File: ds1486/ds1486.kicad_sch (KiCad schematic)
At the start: 13 parts, among them J2 DBG1-16, J3 DBG17-32, J4 DS1-16, J5 DS17-32, U1 RP2040, U2 FXMA108, U3 AMS1117-3.3, Y2 E3SB12E00004EE

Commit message: PCB without RTC and battery.
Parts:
- removed U2: FXMA108, Package_DFN_QFN:WQFN-20-1EP_2.5x4.5mm_P0.5mm_EP1x2.9mm, symbol Logic_LevelTranslator:FXMA108
- added J1: DBG, Connector_PinHeader_2.54mm:PinHeader_1x03_P2.54mm_Vertical, symbol Connector:Conn_01x03_Pin
- added R10, R11, R12, R13, R14, R15, R16, R17, R18, R19, R2, R4, R5, R6, R7, R8, R9: R, Resistor_SMD:R_0402_1005Metric_Pad0.72x0.64mm_HandSolder, symbol Device:R
- added U2: W25X20CLSNIG, Package_SO:SOIC-8_5.3x5.3mm_P1.27mm, symbol Kicad_Personal:W25X20CLSNIG
- added U4: SN74LVC8T245, Package_SO:SSOP-24_3.9x8.7mm_P0.635mm, symbol Logic_LevelTranslator:SN74LVC8T245
- added U5, U7: SN74LVC1G00DRL, Package_TO_SOT_SMD:Texas_R-PDSO-N5_DRL-5, symbol 74xGxx:SN74LVC1G00DRL
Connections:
- net +3V3: now also U2.8 (VCC), U4.1 (V_{CCA}), U5.5 (VCC), U7.5 (VCC)
- net +5V: now also U4.23 (V_{CCB}), U4.24 (V_{CCB})
- net A0: now also R2.1
- net A1: now also R4.1
- net A10: now also R16.1
- net A11: now also R15.1
- net A12: now also R14.1
- net A13: now also R13.1
- net A14: now also R12.1
- net A15: now also R11.1
- net A16: now also R19.1
- net A2: now also R6.1
- net A3: now also R5.1
- net A4: now also R8.1
- net A5: now also R7.1
- net A6: now also R10.1
- net A7: now also R9.1
- net A8: now also R18.1
- net A9: now also R17.1
- net CE_: now also U5.1, U7.1
- net DQ0: now also U4.21 (B1)
- net DQ1: now also U4.20 (B2)
- net DQ2: now also U4.19 (B3)
- net DQ3: now also U4.14 (B8)
- net DQ4: now also U4.15 (B7)
- net DQ5: now also U4.16 (B6)
- net DQ6: now also U4.17 (B5)
- net DQ7: now also U4.18 (B4)
- net GND: now also U1.40 (GPIO28_ADC2), U1.57 (GND), J1.2 (Pin_2), U2.4 (GND), U4.11 (GND), U4.12 (GND), U4.13 (GND), U4.2 (DIR), U4.22 (~{OE}), U5.3 (GND), U7.3 (GND)
- net OE_: now also U7.2
- net WE_: now also U5.2
- net AC12: now reaches U1.11 (GPIO8)
- net AC12: now also R14.2
- net AC14: now reaches U1.12 (GPIO9)
- net AC14: now also R12.2
- net AC16: now reaches U1.13 (GPIO10)
- net AC16: now also R19.2
- net AC15: now reaches U1.14 (GPIO11)
- net AC15: now also R11.2
- net AC13: now reaches U1.15 (GPIO12)
- net AC13: now also R13.2
- net AC8: now reaches U1.16 (GPIO13)
- net AC8: now also R18.2
- net AC9: now reaches U1.17 (GPIO14)
- net AC9: now also R17.2
- net AC11: now reaches U1.18 (GPIO15)
- net AC11: now also R15.2
- net AC0: now reaches U1.2 (GPIO0)
- net AC0: now also R2.2
- net SWCLK: now reaches U1.24 (SWCLK)
- net SWCLK: now also J1.1 (Pin_1)
- net SWD: now reaches U1.25 (SWD)
- net SWD: now also J1.3 (Pin_3)
- net AC10: now reaches U1.27 (GPIO16)
- net AC10: now also R16.2
- net CE_OE: now reaches U1.28 (GPIO17)
- net CE_OE: now also U7.4
- net CE_WE: now reaches U1.29 (GPIO18)
- net CE_WE: now also U5.4
- net AC1: now reaches U1.3 (GPIO1)
- net AC1: now also R4.2
- net DQC0: now reaches U1.31 (GPIO20)
- net DQC0: now also U4.3 (A1)
- net DQC1: now reaches U1.32 (GPIO21)
- net DQC1: now also U4.4 (A2)
- net DQC2: now reaches U1.34 (GPIO22)
- net DQC2: now also U4.5 (A3)
- net DQC3: now reaches U1.35 (GPIO23)
- net DQC3: now also U4.10 (A8)
- net DQC4: now reaches U1.36 (GPIO24)
- net DQC4: now also U4.9 (A7)
- net DQC5: now reaches U1.37 (GPIO25)
- net DQC5: now also U4.8 (A6)
- net DQC6: now reaches U1.38 (GPIO26_ADC0)
- net DQC6: now also U4.7 (A5)
- net DQC7: now reaches U1.39 (GPIO27_ADC1)
- net DQC7: now also U4.6 (A4)
- net AC2: now reaches U1.4 (GPIO2)
- net AC2: now also R6.2
- net AC3: now reaches U1.5 (GPIO3)
- net AC3: now also R5.2
- net QSPI_SD3: now reaches U1.51 (QSPI_SD3)
- net QSPI_SD3: now also U2.7 (~{HOLD}/~{RESET}/IO_{3})
- net QSPI_SCLK: now reaches U1.52 (QSPI_SCLK)
- net QSPI_SCLK: now also U2.6 (CLK)
- net QSPI_SD0: now reaches U1.53 (QSPI_SD0)
- net QSPI_SD0: now also U2.5 (DI/IO_{0})
- net QSPI_SD2: now reaches U1.54 (QSPI_SD2)
- net QSPI_SD2: now also U2.3 (~{WP}/IO_{2})
- net QSPI_SD1: now reaches U1.55 (QSPI_SD1)
- net QSPI_SD1: now also U2.2 (DO/IO_{1})
- net QSPI_SS: now reaches U1.56 (QSPI_SS)
- net QSPI_SS: now also U2.1 (~{CS})
- net AC4: now reaches U1.6 (GPIO4)
- net AC4: now also R8.2
- net AC5: now reaches U1.7 (GPIO5)
- net AC5: now also R7.2
- net AC6: now reaches U1.8 (GPIO6)
- net AC6: now also R10.2
- net AC7: now reaches U1.9 (GPIO7)
- net AC7: now also R9.2
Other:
- note added: "DIR is controlled by rp2040 instead of OE_ directly due to 40ns delay requirement between OE_ and driver active."
- note added: "External NAND gates remove requirement to check CE_ explicitly in software and saves an instruction."
- moved on the sheet: C1, C2, C3, C4, R1, U1, U3, Y2

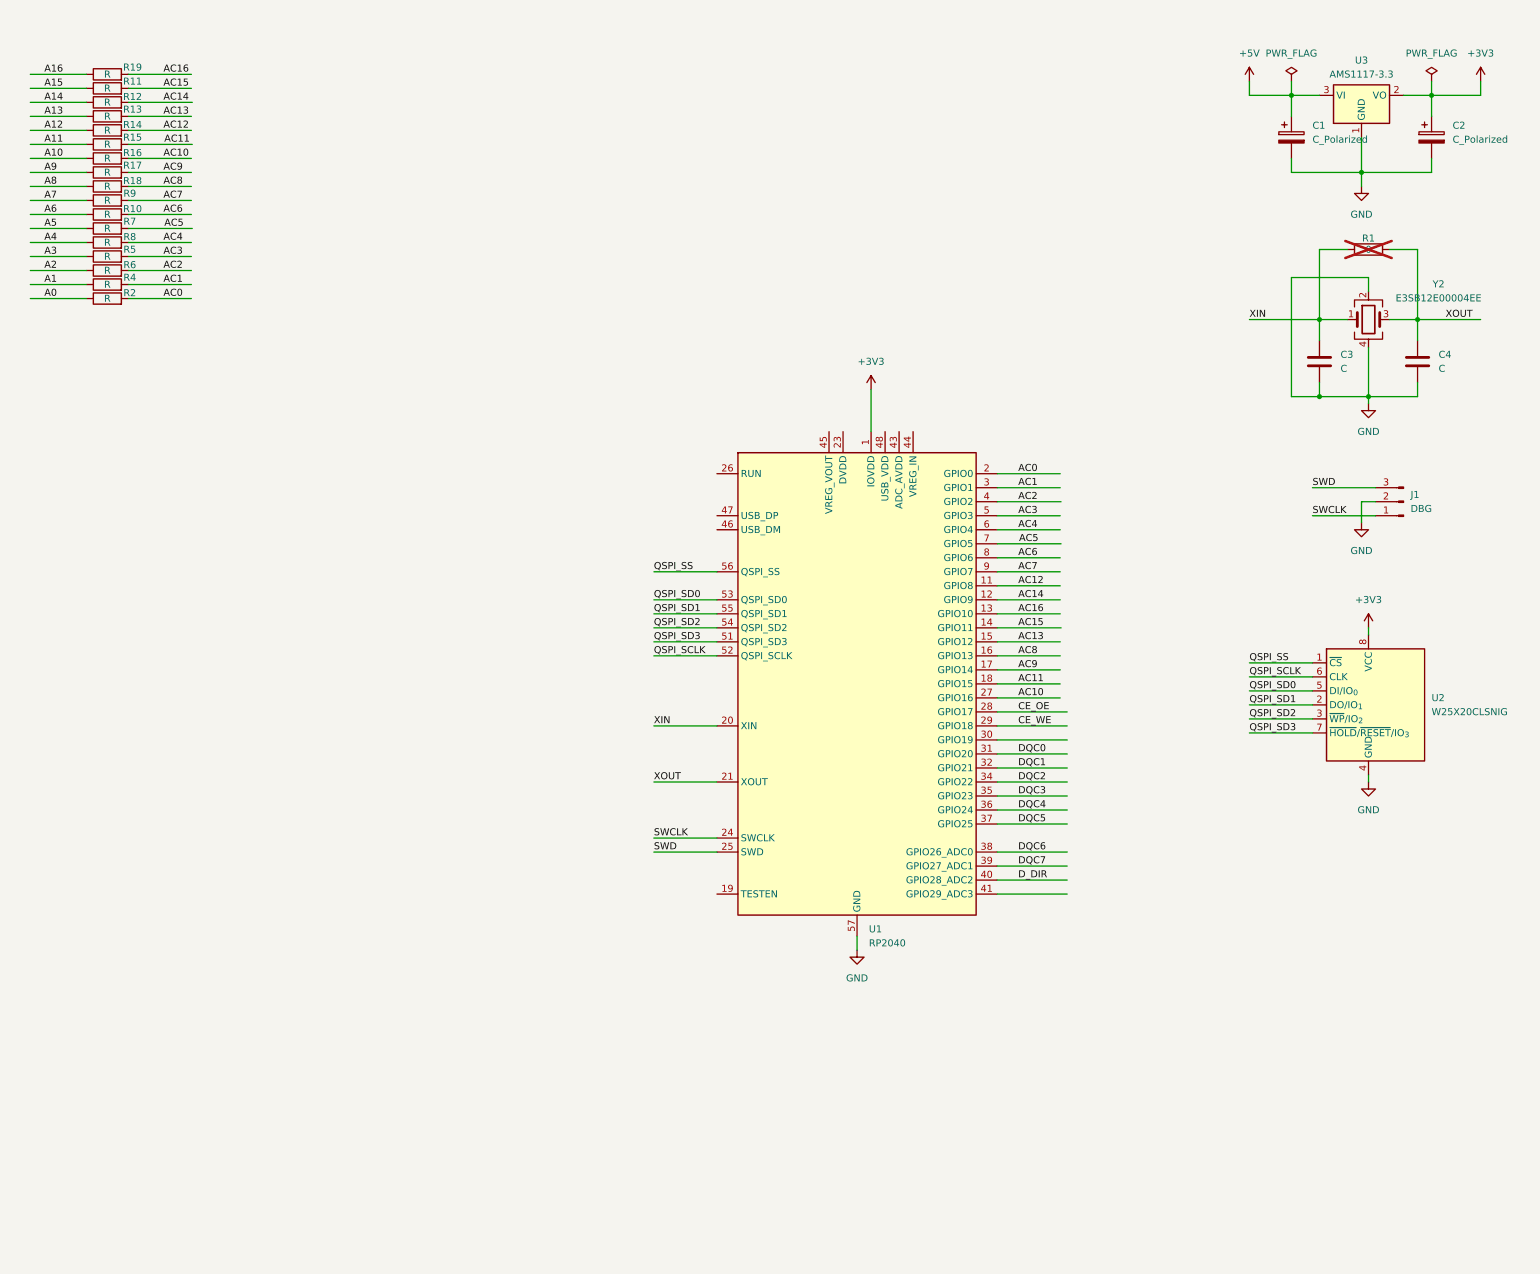
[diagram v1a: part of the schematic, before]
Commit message: Add RTC.
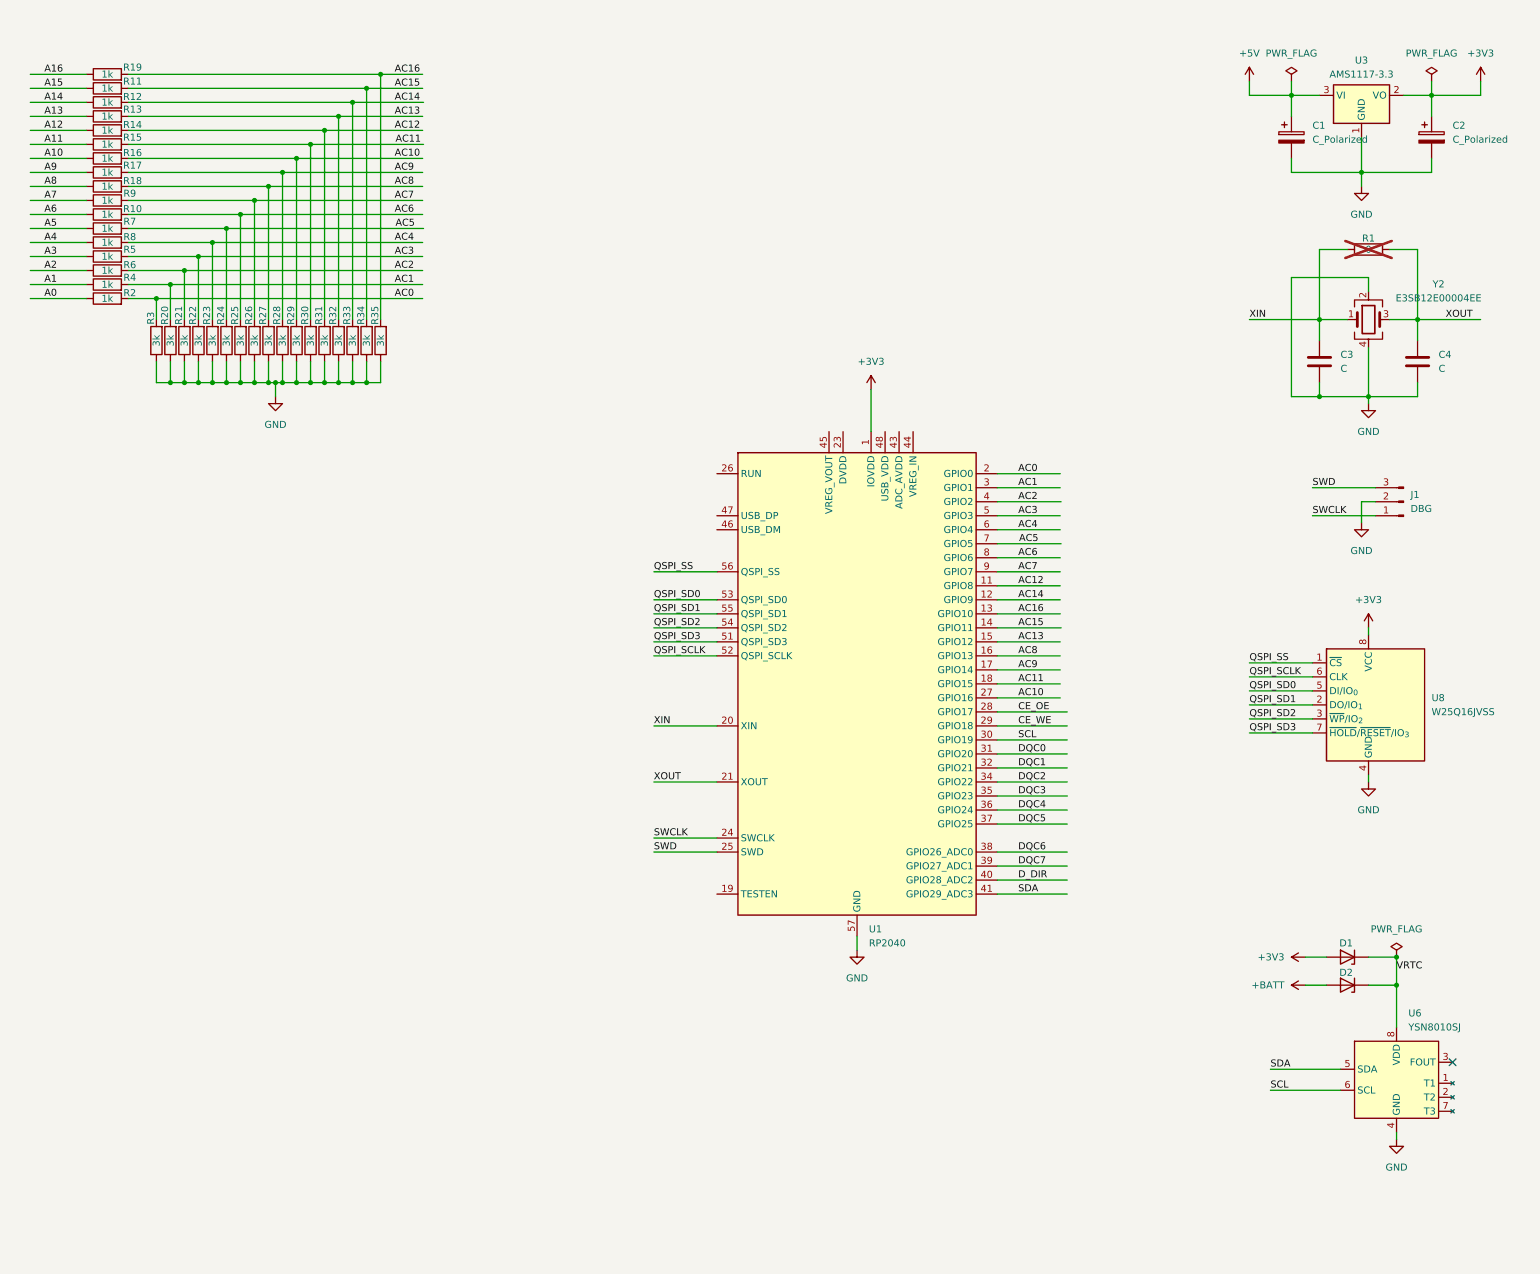
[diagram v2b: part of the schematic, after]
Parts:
- removed U2: W25X20CLSNIG, Package_SO:SOIC-8_5.3x5.3mm_P1.27mm, symbol Kicad_Personal:W25X20CLSNIG
- added D1, D2: BZT52C6V8-7-F, Diode_SMD:D_SOD-123F, symbol Diode:BZT52Bxx
- added R20, R21, R22, R23, R24, R25, R26, R27, R28, R29, R3, R30, R31, R32, R33, R34, R35: 3k, Resistor_SMD:R_0402_1005Metric, symbol Device:R
- added U6: YSN8010SJ, Package_SO:SOP-8_3.9x4.9mm_P1.27mm, symbol Kicad_Personal:YSN8010SJ
- added U8: W25Q16JVSS, Package_SO:SOIC-8_5.3x5.3mm_P1.27mm, symbol Memory_Flash:W25Q16JVSS
- R10, R11, R12, R13, R14, R15, R16, R17, R18, R19, R2, R4, R5, R6, R7, R8, R9: value R -> 1k; footprint Resistor_SMD:R_0402_1005Metric_Pad0.72x0.64mm_HandSolder -> Resistor_SMD:R_0402_1005Metric
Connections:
- net +3V3: now also D1.2 (A), U8.8 (VCC)
- net AC0: now also R3.2
- net AC1: now also R20.2
- net AC10: now also R29.2
- net AC11: now also R30.2
- net AC12: now also R31.2
- net AC13: now also R32.2
- net AC14: now also R33.2
- net AC15: now also R34.2
- net AC16: now also R35.2
- net AC2: now also R21.2
- net AC3: now also R22.2
- net AC4: now also R23.2
- net AC5: now also R24.2
- net AC6: now also R25.2
- net AC7: now also R26.2
- net AC8: now also R27.2
- net AC9: now also R28.2
- net GND: now also R20.1, R21.1, R22.1, R23.1, R24.1, R25.1, R26.1, R27.1, R28.1, R29.1, R3.1, R30.1, R31.1, R32.1, R33.1, R34.1, R35.1, U6.4 (GND), U8.4 (GND)
- net QSPI_SCLK: now also U8.6 (CLK)
- net QSPI_SD0: now also U8.5 (DI/IO_{0})
- net QSPI_SD1: now also U8.2 (DO/IO_{1})
- net QSPI_SD2: now also U8.3 (~{WP}/IO_{2})
- net QSPI_SD3: now also U8.7 (~{HOLD}/~{RESET}/IO_{3})
- net QSPI_SS: now also U8.1 (~{CS})
- net SCL: now reaches U1.30 (GPIO19)
- net SCL: now also U6.6 (SCL)
- net SDA: now reaches U1.41 (GPIO29_ADC3)
- net SDA: now also U6.5 (SDA)
- new net +BATT: D2.2 (A)
- new net VRTC: D1.1 (K), D2.1 (K), U6.8 (VDD)
- no-connect marks 0 -> 1

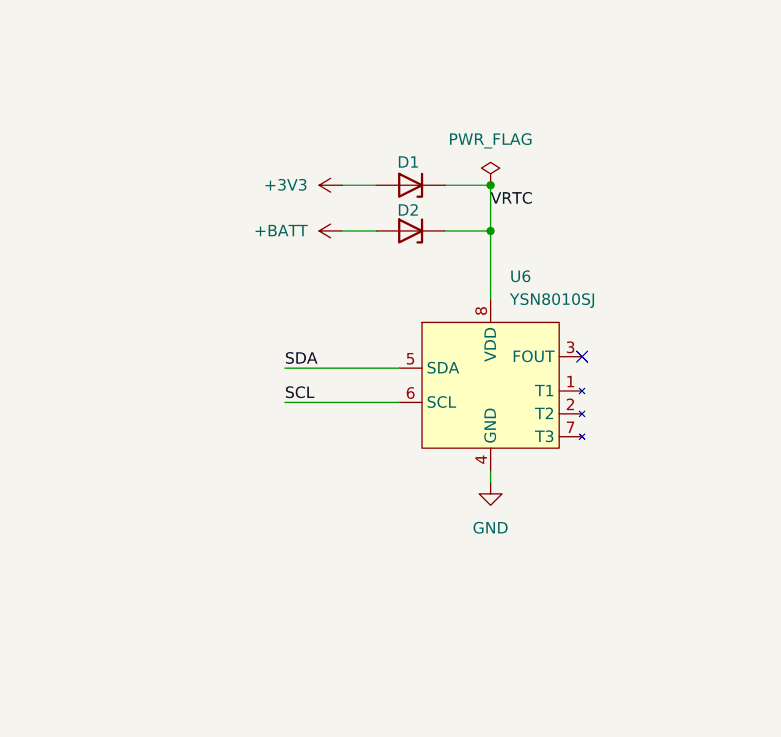
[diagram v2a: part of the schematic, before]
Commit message: Add battery and narrow pin header.
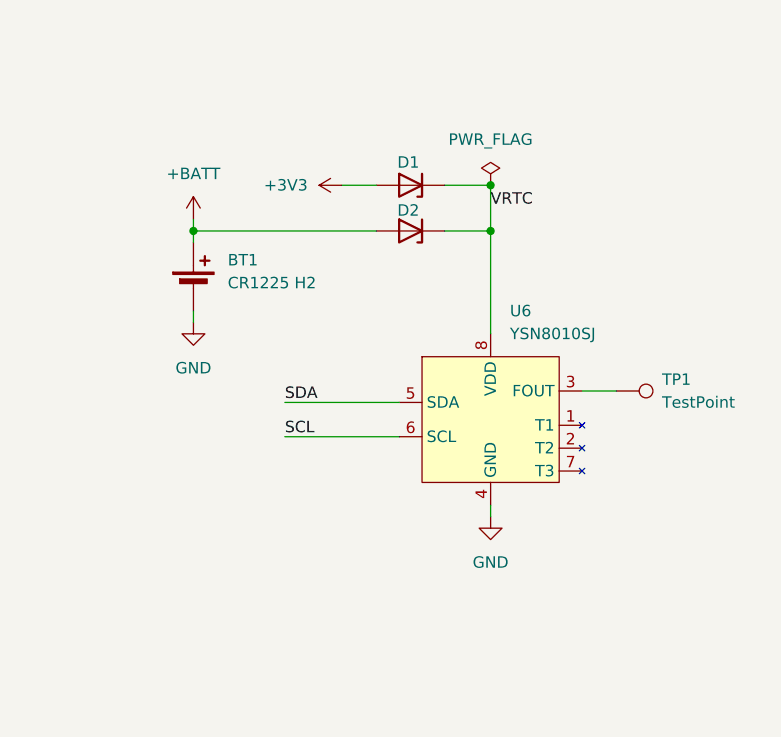
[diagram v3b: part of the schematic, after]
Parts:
- added BT1: CR1225 H2, Kicad_Personal:CR1225_H2, symbol Device:Battery_Cell
- added TP1: TestPoint, symbol Connector:TestPoint
- J4, J5: footprint Connector_PinHeader_2.54mm:PinHeader_1x16_P2.54mm_Vertical -> Kicad_Personal:PinHeader_1x16_P2.54mm_Vertical_DIP_Diameter_Flipside
- Y2: footprint Crystal:Crystal_SMD_3225-4Pin_3.2x2.5mm_HandSoldering -> Crystal:Crystal_SMD_3225-4Pin_3.2x2.5mm
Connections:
- net +BATT: now also BT1.1 (+)
- net GND: now also BT1.2 (-)
- net at U6.3 (FOUT): now also TP1.1
- no-connect marks 1 -> 0
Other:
- moved on the sheet: U6

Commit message: Fully routed.
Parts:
- added C10, C13, C14, C15, C16, C17, C5, C6, C7, C8, C9: 100n, Capacitor_SMD:C_0603_1608Metric, symbol Device:C
- added C11, C12: 1u, Capacitor_SMD:C_0603_1608Metric, symbol Device:C
- added R36: 10k, Resistor_SMD:R_0402_1005Metric, symbol Device:R
- added R37, R38: 4k7, Resistor_SMD:R_0603_1608Metric, symbol Device:R
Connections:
- net +3V3: now also U1.43 (ADC_AVDD), U1.44 (VREG_IN), U1.48 (USB_VDD), C10.1, C11.1, C15.1, C17.1, C5.1, C6.1, C7.1, C8.1, C9.1, R36.2, R37.2, R38.2
- net +5V: now also C16.1
- net AC0: now also U1.38 (GPIO26_ADC0); no longer U1.2 (GPIO0)
- net AC1: now also U1.39 (GPIO27_ADC1); no longer U1.3 (GPIO1)
- net AC10: now also U1.16 (GPIO13); no longer U1.27 (GPIO16)
- net AC11: now also U1.17 (GPIO14); no longer U1.18 (GPIO15)
- net AC12: now also U1.32 (GPIO21); no longer U1.11 (GPIO8)
- net AC13: now also U1.28 (GPIO17); no longer U1.15 (GPIO12)
- net AC14: now also U1.31 (GPIO20); no longer U1.12 (GPIO9)
- net AC15: now also U1.29 (GPIO18); no longer U1.14 (GPIO11)
- net AC16: now also U1.30 (GPIO19); no longer U1.13 (GPIO10)
- net AC2: now also U1.40 (GPIO28_ADC2); no longer U1.4 (GPIO2)
- net AC3: now also U1.41 (GPIO29_ADC3); no longer U1.5 (GPIO3)
- net AC4: now also U1.37 (GPIO25); no longer U1.6 (GPIO4)
- net AC5: now also U1.36 (GPIO24); no longer U1.7 (GPIO5)
- net AC6: now also U1.35 (GPIO23); no longer U1.8 (GPIO6)
- net AC7: now also U1.34 (GPIO22); no longer U1.9 (GPIO7)
- net AC8: now also U1.27 (GPIO16); no longer U1.16 (GPIO13)
- net AC9: now also U1.18 (GPIO15); no longer U1.17 (GPIO14)
- net CE_OE: now also U1.15 (GPIO12); no longer U1.28 (GPIO17)
- net CE_WE: now also U1.14 (GPIO11); no longer U1.29 (GPIO18)
- net DQC0: now also U1.3 (GPIO1); no longer U1.31 (GPIO20)
- net DQC1: now also U1.4 (GPIO2); no longer U1.32 (GPIO21)
- net DQC2: now also U1.5 (GPIO3); no longer U1.34 (GPIO22)
- net DQC3: now also U1.6 (GPIO4); no longer U1.35 (GPIO23)
- net DQC4: now also U1.7 (GPIO5); no longer U1.36 (GPIO24)
- net DQC5: now also U1.8 (GPIO6); no longer U1.37 (GPIO25)
- net DQC6: now also U1.9 (GPIO7); no longer U1.38 (GPIO26_ADC0)
- net DQC7: now also U1.11 (GPIO8); no longer U1.39 (GPIO27_ADC1)
- net GND: now also U1.19 (TESTEN), C10.2, C11.2, C12.2, C13.2, C14.2, C15.2, C16.2, C17.2, C5.2, C6.2, C7.2, C8.2, C9.2; no longer U1.40 (GPIO28_ADC2), U4.2 (DIR)
- net SCL: now also U1.12 (GPIO9), R37.1; no longer U1.30 (GPIO19)
- net SDA: now also U1.13 (GPIO10), R38.1; no longer U1.41 (GPIO29_ADC3)
- net +1V1: now reaches U1.23 (DVDD), U1.50 (DVDD)
- net +1V1: now also U1.45 (VREG_VOUT), C12.1, C13.1, C14.1
- net RUN: now reaches U1.26 (RUN)
- net RUN: now also R36.1
- new net D_DIR: U1.2 (GPIO0), U4.2 (DIR)
- no-connect marks 0 -> 2
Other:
- note added: "1 cap for each IOVDD pin"
- note added: "VDD"
- note added: "VREG_VIN"
- note added: "VREG_VOUT"
- moved on the sheet: BT1

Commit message: Add some decoupling caps. Gerbers.
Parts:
- removed TP1: TestPoint, symbol Connector:TestPoint
- added C18, C19: 100n, Capacitor_SMD:C_0402_1005Metric, symbol Device:C
- added C20: 100n, Capacitor_SMD:C_0603_1608Metric, symbol Device:C
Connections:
- net +3V3: now also C18.1, C19.1
- net GND: now also C18.2, C19.2, C20.2
- net VRTC: now also C20.1
- no-connect marks 2 -> 3
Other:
- moved on the sheet: U6
